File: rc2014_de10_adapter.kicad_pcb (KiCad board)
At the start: 2 copper layers, 101.6 x 50.8 mm, 27 parts, among them J1 Conn_02x20_Odd_Even, J2 Conn_01x10_Male, J3 Conn_01x08_Male, J4 M3 Mounting Hole, J5 Z80 Bus, J6 Pro Bus, U1 SN74LVC245A, U10 MAX40200AUK, U2 SN74LVC245A, U3 SN74LVC245A, U4 SN74LVC245A, U5 SN74LVC245A, U6 AZ1117-3.3, U7 MAX40200AUK, U8 MAX40200AUK, U9 MAX40200AUK

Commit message: finished routing
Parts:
- removed the C4 at (111.8, 119.0)
- removed the C6 at (100.5, 93.2)
- removed the U6 at (111.4, 108.9)
- removed the U7 at (111.8, 122.1)
- removed the U8 at (100.6, 86.4)
- added C1: 100nF, Capacitor_SMD:C_0805_2012Metric_Pad1.15x1.40mm_HandSolder, F.Cu at (119.9, 120.4)
- added C3: 100nF, Capacitor_SMD:C_0805_2012Metric_Pad1.15x1.40mm_HandSolder, F.Cu at (147.1, 116.1)
- added C8: 100nF, Capacitor_SMD:C_0805_2012Metric_Pad1.15x1.40mm_HandSolder, F.Cu at (115.8, 98.6)
- added U1: AZ1117-3.3, Package_TO_SOT_SMD:SOT-223-3_TabPin2, F.Cu at (109.5, 112.3)
- C10: renamed from C9; moved to F.Cu
- C11, C2, C7: moved to F.Cu
- C12: renamed from C10; moved to F.Cu
- C4: renamed from C1; moved to F.Cu
- C5: value 1uF -> 100nF; moved to F.Cu
- C6: renamed from C3; moved to F.Cu
- C9: renamed from C8; moved to F.Cu
- U2: renamed from U9; moved to F.Cu
- U6: renamed from U10; moved to F.Cu
- moved C4 42.1 mm to (78.0, 116.3), turned to 90 degrees
- moved C5 37.0 mm to (77.7, 102.6), turned to 90 degrees
- moved C7 26.5 mm to (115.8, 112.0), turned to 270 degrees
- moved C11 5.98 mm to (161.6, 86.8), turned to 0 degrees
- moved C12 5.98 mm to (161.6, 84.2), turned to 0 degrees
- moved U6 5.98 mm to (161.6, 80.6), turned to 0 degrees
- moved C10 4.59 mm to (112.0, 96.8), turned to 0 degrees
- moved U8 4.32 mm to (118.6, 102.4)
- moved C2 4.00 mm to (111.5, 118.1)
- moved C6 3.58 mm to (111.5, 107.2)
- moved U3 3.36 mm to (149.6, 119.9)
- moved U7 2.03 mm to (118.6, 116.3)
- moved U4 1.52 mm to (80.5, 120.1)
- moved C9 1.48 mm to (112.0, 94.0), turned to 0 degrees
- moved U2 0.77 mm to (112.0, 100.6), turned to 0 degrees
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- renumbered J5 to J1, J6 to J2, J4 to J3, J2 to J4, J1 to J5, J3 to J6, U5 to U3, U1 to U4, U2 to U5, U3 to U7, U4 to U8
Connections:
- C4 pad 2: 5V -> +3V3
- C5 pad 2: 5V -> +3V3
- C7 pad 2: 5V -> +3V3
- J4 pad 10: ~RESETF -> (no net)
- J4 pad 4: (no net) -> GND
- J4 pad 5: (no net) -> PAGEF
- J4 pad 7: GND -> ~INTF
- J4 pad 8: (no net) -> ~NMIF
- J4 pad 9: PAGEF -> (no net)
- J5 pad 1: ~M1F -> A6F
- J5 pad 10: ~NMIF -> A15F
- J5 pad 11: 5VF -> (no net)
- J5 pad 13: A15F -> A12F
- J5 pad 14: A7F -> A13F
- J5 pad 15: A14F -> A10F
- J5 pad 16: A6F -> A11F
- J5 pad 17: A13F -> A8F
- J5 pad 18: A5F -> A9F
- J5 pad 19: A12F -> ~M1F
- J5 pad 2: ~IORQF -> A7F
- J5 pad 20: A4F -> (no net)
- J5 pad 21: A11F -> CLKF
- J5 pad 22: A3F -> ~RESETF
- J5 pad 23: A10F -> ~MREQF
- J5 pad 24: A2F -> ~RDF
- J5 pad 25: A9F -> ~WRF
- J5 pad 26: A1F -> (no net)
- J5 pad 27: A8F -> ~IORQF
- J5 pad 28: A0F -> (no net)
- J5 pad 3: CLKF -> A4F
- J5 pad 31: D0F -> (no net)
- J5 pad 32: D4F -> (no net)
- J5 pad 33: D1F -> D0F
- J5 pad 34: D5F -> D1F
- J5 pad 36: D6F -> D3F
- J5 pad 37: D3F -> D4F
- J5 pad 38: D7F -> D5F
- J5 pad 39: ~WAITF -> D6F
- J5 pad 4: ~BUSACKF -> A5F
- J5 pad 40: ~INTF -> D7F
- J5 pad 5: ~MREQF -> A2F
- J5 pad 6: ~HALTF -> A3F
- J5 pad 7: ~WRF -> A0F
- J5 pad 8: ~BUSRQF -> A1F
- J5 pad 9: ~RDF -> A14F
- J6 pad 1: RxF -> ~HALTF
- J6 pad 2: TxF -> ~BUSRQF
- J6 pad 3: (no net) -> ~WAITF
- J6 pad 4: (no net) -> ~BUSACKF
- J6 pad 6: (no net) -> DIR
- J6 pad 7: (no net) -> RxF
- J6 pad 8: DIR -> TxF
- U8 pad 12: PAGEF -> ~WAITF
- U8 pad 13: ~WAITF -> ~BUSRQF
- U8 pad 14: ~INTF -> ~HALTF
- U8 pad 17: ~BUSRQF -> ~INTF
- U8 pad 18: ~HALTF -> PAGEF
- U8 pad 2: ~HALT -> PAGE
- U8 pad 3: ~BUSRQ -> ~INT
- U8 pad 6: ~INT -> ~HALT
- U8 pad 7: ~WAIT -> ~BUSRQ
- U8 pad 8: PAGE -> ~WAIT
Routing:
- net GND: track 0.00 -> 430.6 mm, vias 0 -> 4
- net +3V3: track 0.00 -> 207.8 mm
- net A15F: track 0.00 -> 59.8 mm
- net A13F: track 0.00 -> 55.3 mm
- net ~NMI: track 0.00 -> 54.4 mm
- net A14F: track 0.00 -> 50.1 mm
- net A11F: track 0.00 -> 49.5 mm
- net A9F: track 0.00 -> 47.4 mm
- net A10F: track 0.00 -> 47.3 mm
- net Rx: track 0.00 -> 46.9 mm
- net A12F: track 0.00 -> 46.7 mm
- net A8F: track 0.00 -> 46.1 mm
- net ~RESET: track 0.00 -> 45.0 mm
- net D1F: track 0.00 -> 41.7 mm
- net DIR: track 0.00 -> 41.1 mm
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
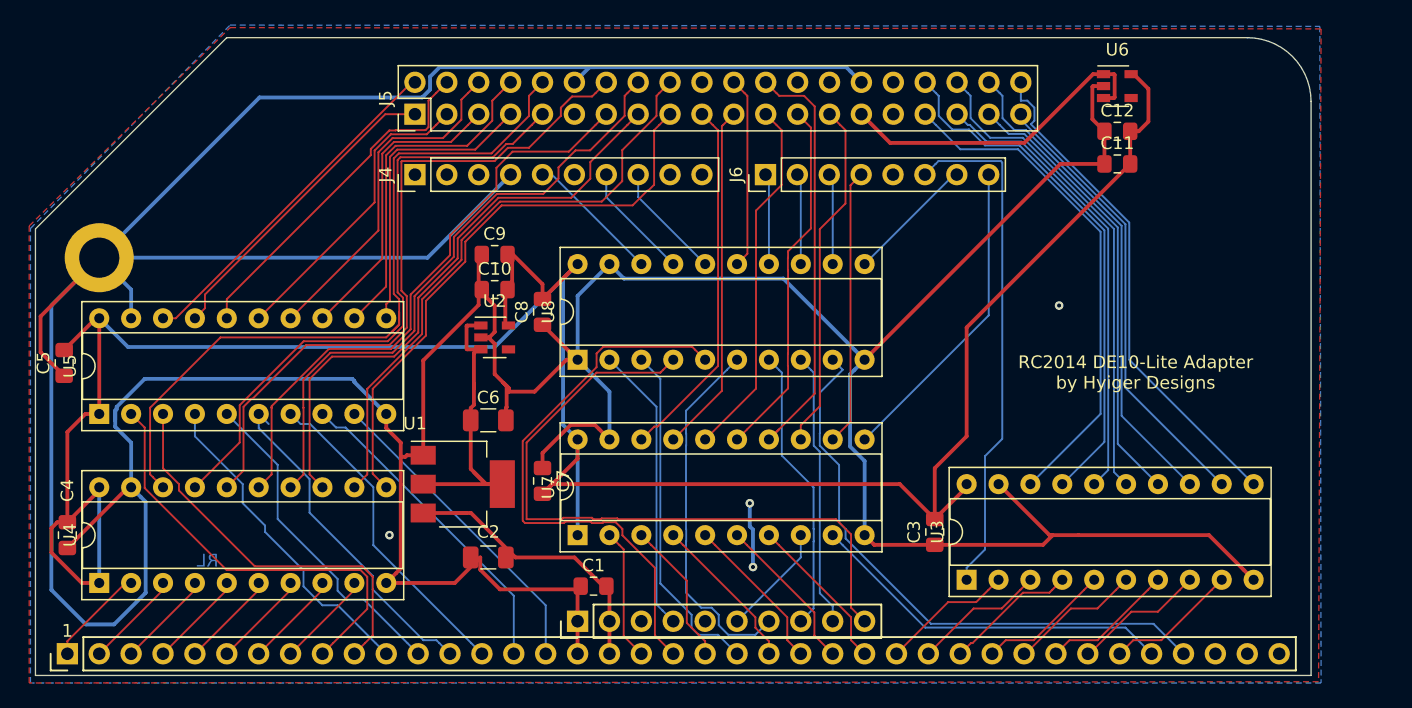
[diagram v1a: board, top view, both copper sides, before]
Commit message: Added FTDI header
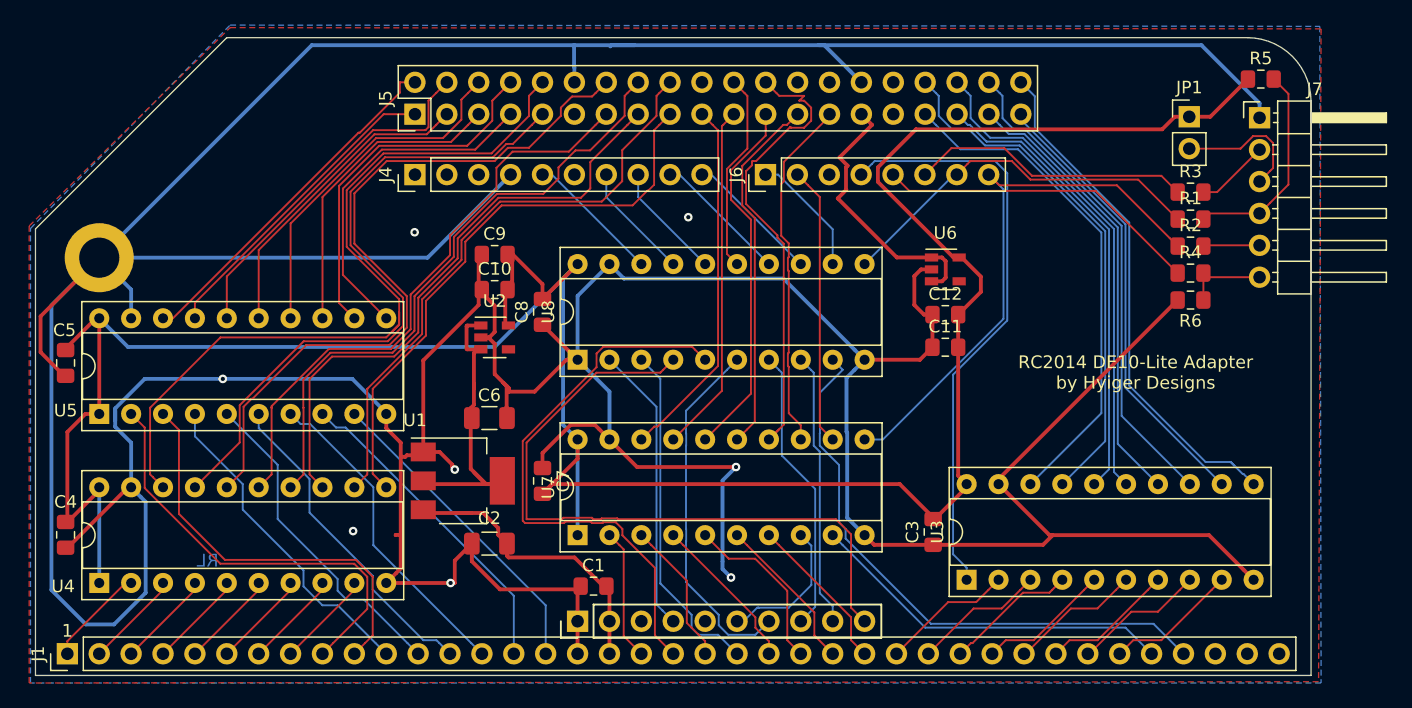
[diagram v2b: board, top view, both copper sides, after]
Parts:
- added J7: FTDI, Connector_PinHeader_2.54mm:PinHeader_1x06_P2.54mm_Horizontal, F.Cu at (172.9, 83.1)
- added JP1: Jumper, Connector_PinHeader_2.54mm:PinHeader_1x02_P2.54mm_Vertical, F.Cu at (167.3, 83.0)
- added R1: 2k2, Resistor_SMD:R_0805_2012Metric_Pad1.15x1.40mm_HandSolder, F.Cu at (167.4, 91.2)
- added R2: 2k2, Resistor_SMD:R_0805_2012Metric_Pad1.15x1.40mm_HandSolder, F.Cu at (167.4, 93.3)
- added R3: 2k2, Resistor_SMD:R_0805_2012Metric_Pad1.15x1.40mm_HandSolder, F.Cu at (167.4, 89.0)
- added R4: 2k2, Resistor_SMD:R_0805_2012Metric_Pad1.15x1.40mm_HandSolder, F.Cu at (167.4, 95.5)
- added R5: 100K, Resistor_SMD:R_0805_2012Metric_Pad1.15x1.40mm_HandSolder, F.Cu at (173.0, 80.0)
- added R6: 100K, Resistor_SMD:R_0805_2012Metric_Pad1.15x1.40mm_HandSolder, F.Cu at (167.4, 97.6)
- moved C12 20.0 mm to (147.9, 98.8)
- moved C11 20.0 mm to (147.9, 101.4)
- moved U6 20.0 mm to (147.9, 95.2)
- moved C2 1.11 mm to (111.6, 117.0)
- moved U1 0.26 mm to (109.5, 112.0)
- moved C6 0.20 mm to (111.6, 107.0)
- moved C4 0.14 mm to (77.8, 116.3)
- moved C3 0.13 mm to (146.9, 116.1)
- moved C5 0.11 mm to (77.8, 102.6)
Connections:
- J4 pad 10: (no net) -> ~BUSRQF
- J4 pad 9: (no net) -> ~HALTF
- J6 pad 1: ~HALTF -> ~WAITF
- J6 pad 2: ~BUSRQF -> ~BUSACKF
- J6 pad 3: ~WAITF -> (no net)
- J6 pad 4: ~BUSACKF -> DIR
- J6 pad 5: (no net) -> ~CTSF
- J6 pad 6: DIR -> ~RTSF
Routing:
- net GND: track 430.6 -> 495.5 mm, vias 4 -> 8
- net ~CTSF: track 0.00 -> 25.9 mm
- net ~RTSF: track 0.00 -> 22.5 mm
- net RxF: track 10.3 -> 30.2 mm
- net TxF: track 25.2 -> 44.4 mm
- net Net-(J7-Pad4): track 0.00 -> 16.8 mm
- net Net-(J7-Pad3): track 0.00 -> 10.8 mm
- net +3V3: track 207.8 -> 218.5 mm
- net Net-(J7-Pad6): track 0.00 -> 6.76 mm
- net DIR: track 41.1 -> 47.1 mm
- net Net-(J7-Pad2): track 0.00 -> 5.88 mm
- net Net-(J7-Pad5): track 0.00 -> 4.50 mm
- net 3V3F: track 26.1 -> 22.0 mm
- net A13F: track 55.3 -> 59.1 mm
- net A15F: track 59.8 -> 63.6 mm
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
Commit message: added direction flags for bus transceivers
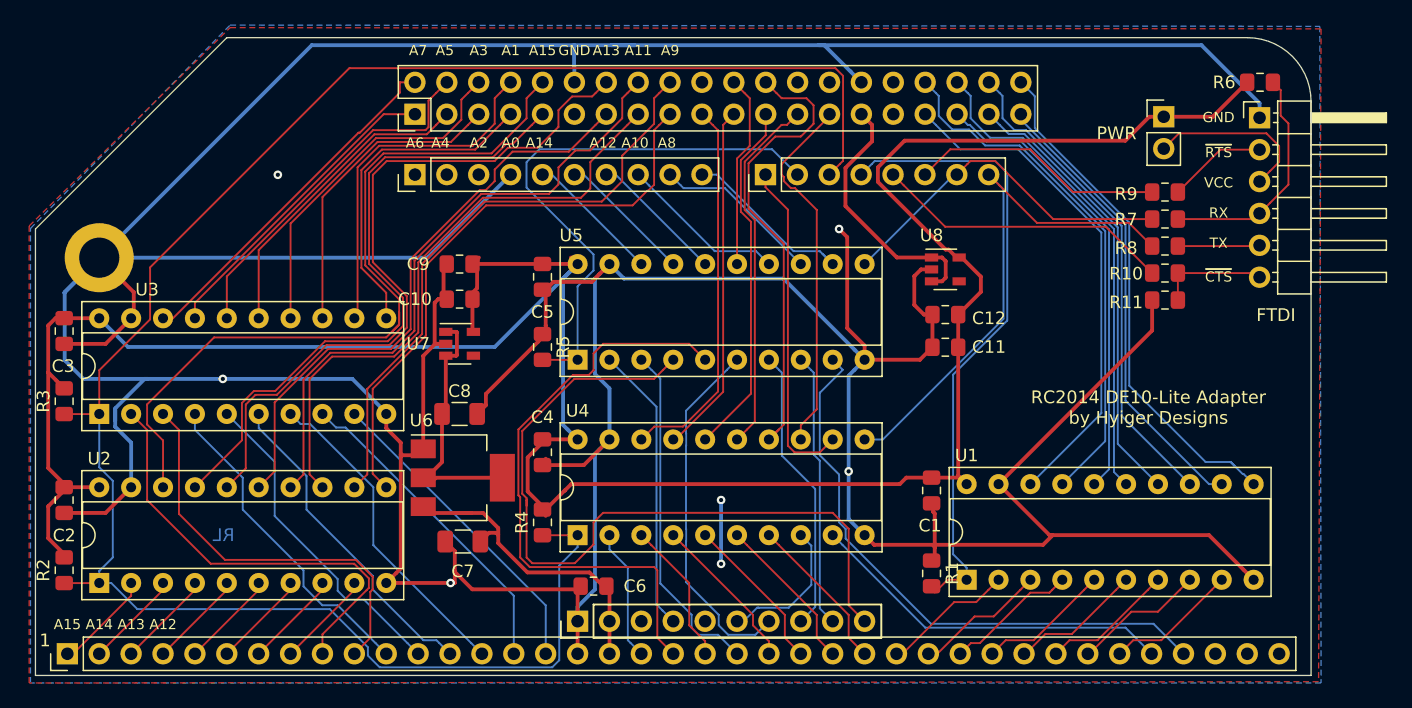
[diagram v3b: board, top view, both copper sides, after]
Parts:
- added R1: 10K, Resistor_SMD:R_0805_2012Metric_Pad1.15x1.40mm_HandSolder, F.Cu at (146.8, 119.4)
- added R2: 10K, Resistor_SMD:R_0805_2012Metric_Pad1.15x1.40mm_HandSolder, F.Cu at (77.7, 119.1)
- added R3: 10K, Resistor_SMD:R_0805_2012Metric_Pad1.15x1.40mm_HandSolder, F.Cu at (77.7, 105.7)
- added R4: 10K, Resistor_SMD:R_0805_2012Metric_Pad1.15x1.40mm_HandSolder, F.Cu at (115.8, 115.3)
- added R5: 10K, Resistor_SMD:R_0805_2012Metric_Pad1.15x1.40mm_HandSolder, F.Cu at (115.8, 101.3)
- moved C1 3.30 mm to (146.8, 112.8)
- moved C10 2.90 mm to (109.2, 97.5)
- moved C9 2.90 mm to (109.2, 94.7)
- moved U7 2.84 mm to (109.2, 101.1)
- moved C5 2.79 mm to (115.8, 95.8)
- moved C2 2.77 mm to (77.7, 113.5)
- moved C3 2.54 mm to (77.7, 100.1)
- moved C8 2.40 mm to (109.2, 106.7)
- moved C4 2.29 mm to (115.8, 109.7), turned to 90 degrees
- moved C7 2.13 mm to (109.5, 116.8)
- moved JP1 2.03 mm to (165.3, 83.0)
- moved R10 2.03 mm to (165.4, 95.5)
- moved R11 2.03 mm to (165.4, 97.6)
- moved R7 2.03 mm to (165.4, 91.2)
- moved R8 2.03 mm to (165.4, 93.3)
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- renumbered C3 to C1, C4 to C2, C5 to C3, C7 to C4, C8 to C5, C1 to C6, C2 to C7, C6 to C8, J5 to J1, J4 to J2, J6 to J3, J1 to J4, J2 to J5, J3 to J6, R4 to R10, R6 to R11, R5 to R6, R1 to R7, R2 to R8, R3 to R9, U3 to U1, U4 to U2, U5 to U3, U7 to U4, U8 to U5, U1 to U6, U2 to U7, U6 to U8
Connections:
- J2 pad 10: ~BUSRQF -> ~WAITF
- J2 pad 6: (no net) -> ~INTF
- J2 pad 7: ~INTF -> ~NMIF
- J2 pad 8: ~NMIF -> ~HALTF
- J2 pad 9: ~HALTF -> ~BUSRQF
- J3 pad 1: ~WAITF -> ~BUSACKF
- J3 pad 2: ~BUSACKF -> ~DIR
- J3 pad 3: (no net) -> DIR
- J3 pad 4: DIR -> ~DBC
- U1 pad 1: DIR -> ~DBC
- U2 pad 1: +3V3 -> DIR
- U3 pad 1: +3V3 -> DIR
- U4 pad 1: +3V3 -> DIR
- U5 pad 1: GND -> ~DIR
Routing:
- net DIR: track 47.1 -> 156.6 mm
- net ~DBC: track 0.00 -> 50.1 mm
- net ~DIR: track 0.00 -> 44.0 mm
- net GND: track 495.5 -> 465.3 mm, vias 8 -> 7
- net ~NMI: track 54.4 -> 62.0 mm
- net +3V3: track 218.5 -> 211.8 mm
- net ~WAITF: track 9.93 -> 14.5 mm
- net ~BUSACKF: track 22.3 -> 26.5 mm
- net 3V3: track 24.4 -> 20.9 mm
- net ~RESET: track 45.0 -> 47.8 mm
- net Net-(J7-Pad3): track 10.8 -> 13.6 mm
- net ~BUSRQF: track 10.8 -> 13.4 mm
- net ~HALTF: track 10.8 -> 13.4 mm
- net ~RTSF: track 22.5 -> 20.3 mm
- net TxF: track 44.4 -> 42.4 mm
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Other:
- board text added: "A0"
- board text added: "A1"
- board text added: "A10"
- board text added: "A11"
- board text added: "A12"
- board text added: "A13"
- board text added: "A14"
- board text added: "A15"
- board text added: "A2"
- board text added: "A3"
- board text added: "A4"
- board text added: "A5"
- board text added: "A6"
- board text added: "A7"
- board text added: "A8"
- board text added: "A9"
- board text added: "FTDI"
- board text added: "GND"
- board text added: "PWR"
- board text added: "RX"
- board text added: "TX"
- board text added: "VCC"
- board text added: "~CTS"
- board text added: "~RTS"

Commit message: fix caps on ideal diodes
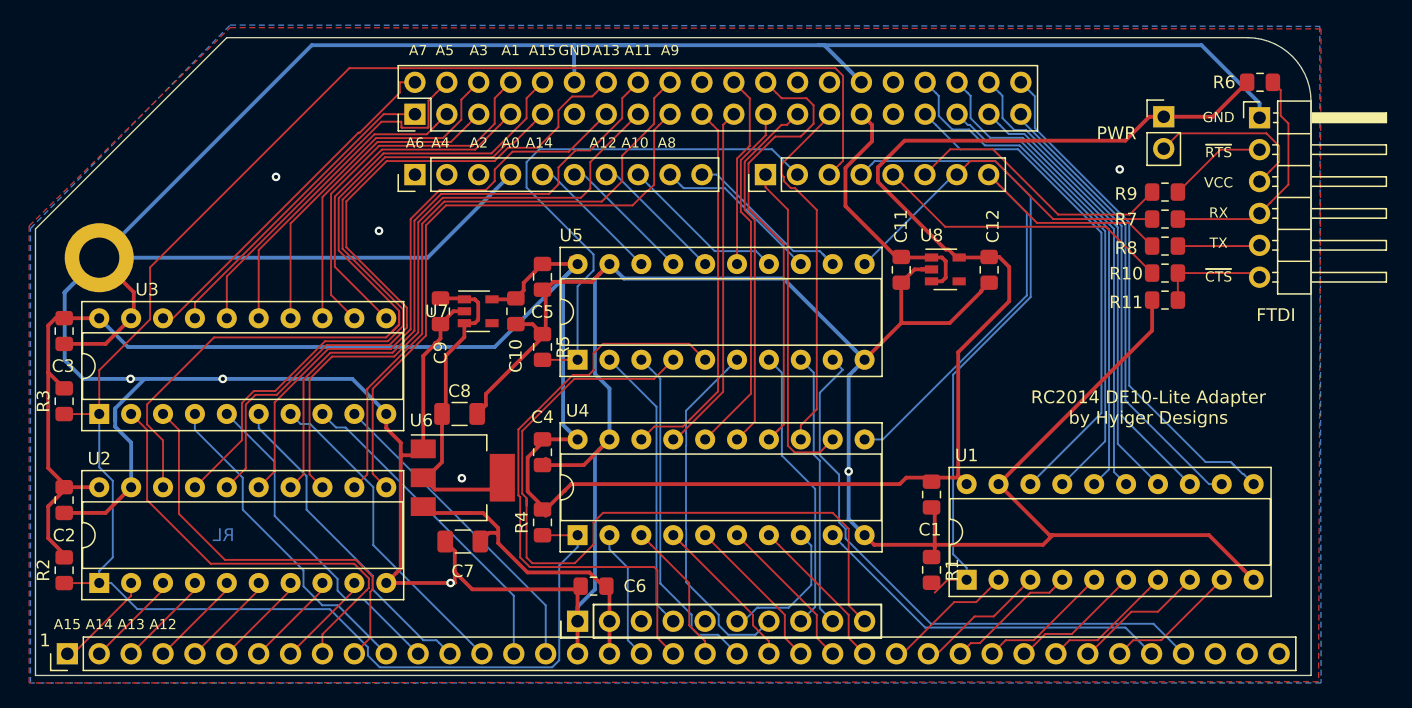
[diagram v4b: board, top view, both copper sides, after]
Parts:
- C11, C9: value 100nF -> 1uF
- moved C11 7.09 mm to (144.4, 95.2), turned to 90 degrees
- moved C12 4.99 mm to (151.4, 95.2), turned to 90 degrees
- moved C10 4.58 mm to (113.7, 98.5), turned to 90 degrees
- moved C9 4.05 mm to (107.7, 98.5), turned to 90 degrees
- moved U7 2.98 mm to (110.7, 98.5)
- moved C1 0.32 mm to (146.8, 113.1)
- moved R1 0.28 mm to (146.8, 119.1)
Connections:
- C11 pad 2: +3V3 -> 3V3F
- C9 pad 2: +3V3 -> 3V3
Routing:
- net GND: track 465.3 -> 452.4 mm, vias 7 -> 8
- net 3V3: track 20.9 -> 26.6 mm
- net +3V3: track 211.8 -> 207.9 mm
- net A12F: track 47.0 -> 48.9 mm
- net A11F: track 50.5 -> 52.3 mm
- net A10F: track 48.5 -> 50.3 mm
- net A9F: track 48.1 -> 50.0 mm
- net A8F: track 46.9 -> 48.7 mm
- net A15F: track 62.9 -> 64.6 mm
- net A0F: track 26.4 -> 28.1 mm
- net A13F: track 58.3 -> 60.1 mm
- net A14F: track 52.7 -> 54.4 mm
- net ~DBC: track 50.1 -> 51.6 mm
- net TxF: track 42.4 -> 43.9 mm
- net A1F: track 28.3 -> 29.9 mm
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
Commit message: fixed cap values
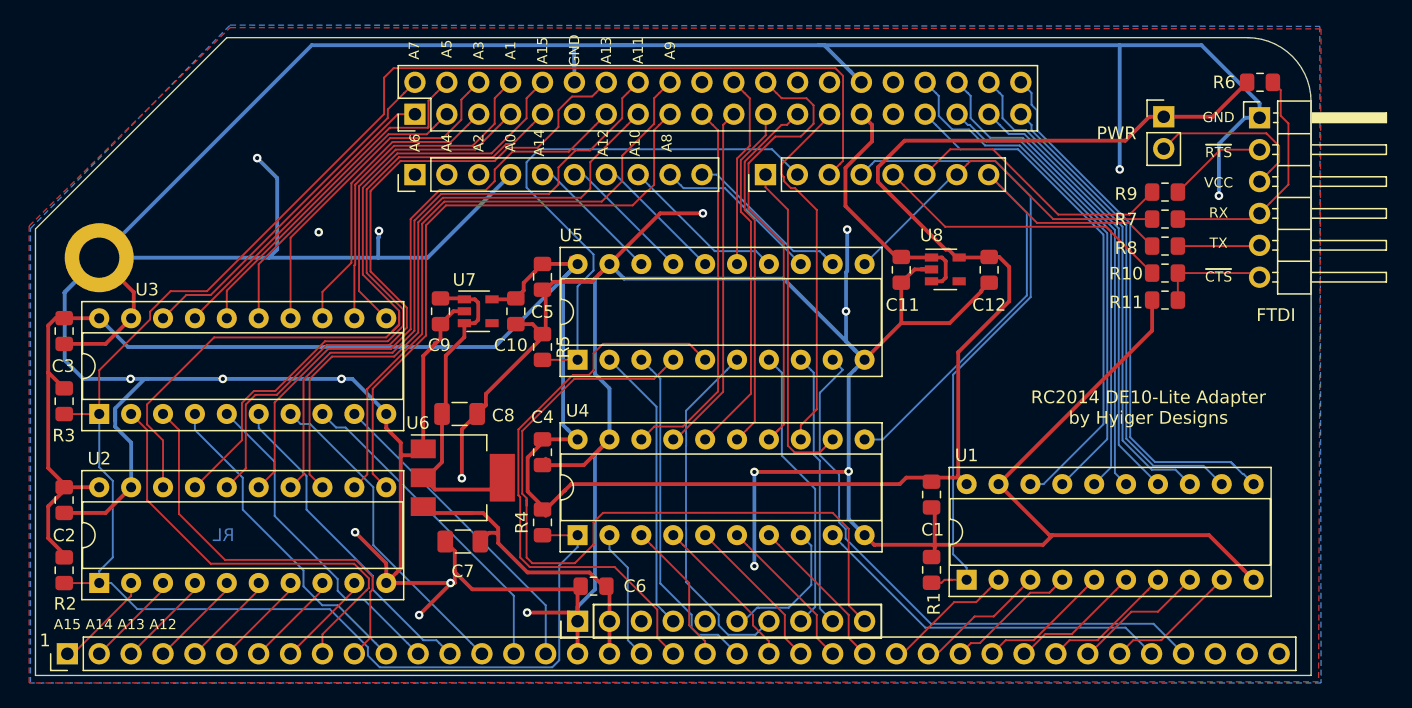
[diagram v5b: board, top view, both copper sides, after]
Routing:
- net GND: track 452.4 -> 535.3 mm, vias 8 -> 19
- net D7F: track 41.3 -> 43.7 mm
- net A0F: track 28.1 -> 25.9 mm
- net A15F: track 64.6 -> 62.4 mm
- net A13F: track 60.1 -> 57.8 mm
- net A14F: track 54.4 -> 52.2 mm
- net A1F: track 29.9 -> 27.6 mm
- net ~RESET: track 47.8 -> 45.9 mm
- net D6F: track 36.7 -> 38.4 mm
- net A5F: track 29.2 -> 27.8 mm
- net D5F: track 39.2 -> 40.3 mm
- net D0F: track 40.3 -> 41.1 mm
- net A2F: track 24.8 -> 24.1 mm
- net A3F: track 28.1 -> 27.5 mm
- net A4F: track 24.9 -> 24.2 mm
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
